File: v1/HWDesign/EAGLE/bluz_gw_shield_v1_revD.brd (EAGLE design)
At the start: 66 x 43.2 mm, 21 parts, among them J2 USB-MICROB, Q1 FC-12M, U2 MDBT40SMD, U3 SST25VF040B-S2, U4 SPARK_CORE

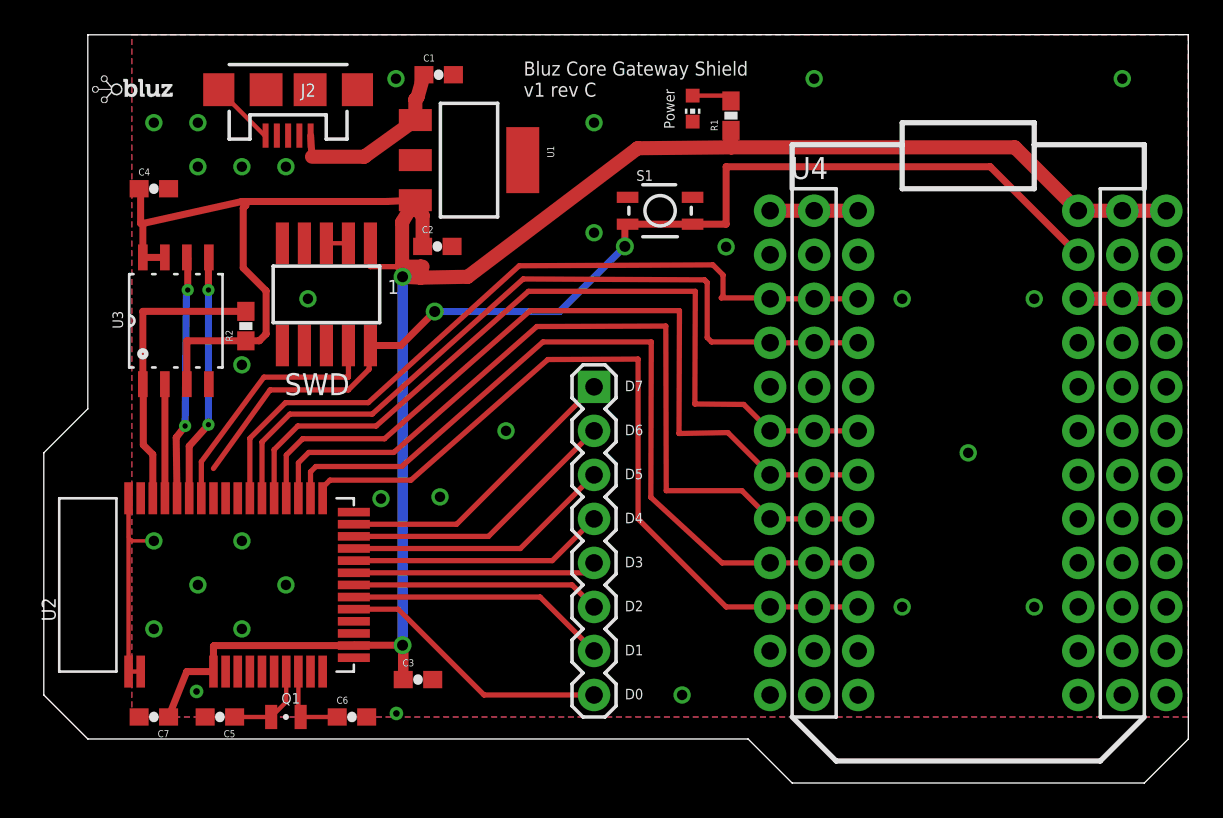
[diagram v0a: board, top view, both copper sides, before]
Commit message: newest files from adding the LED on D7 and TX/RX pins
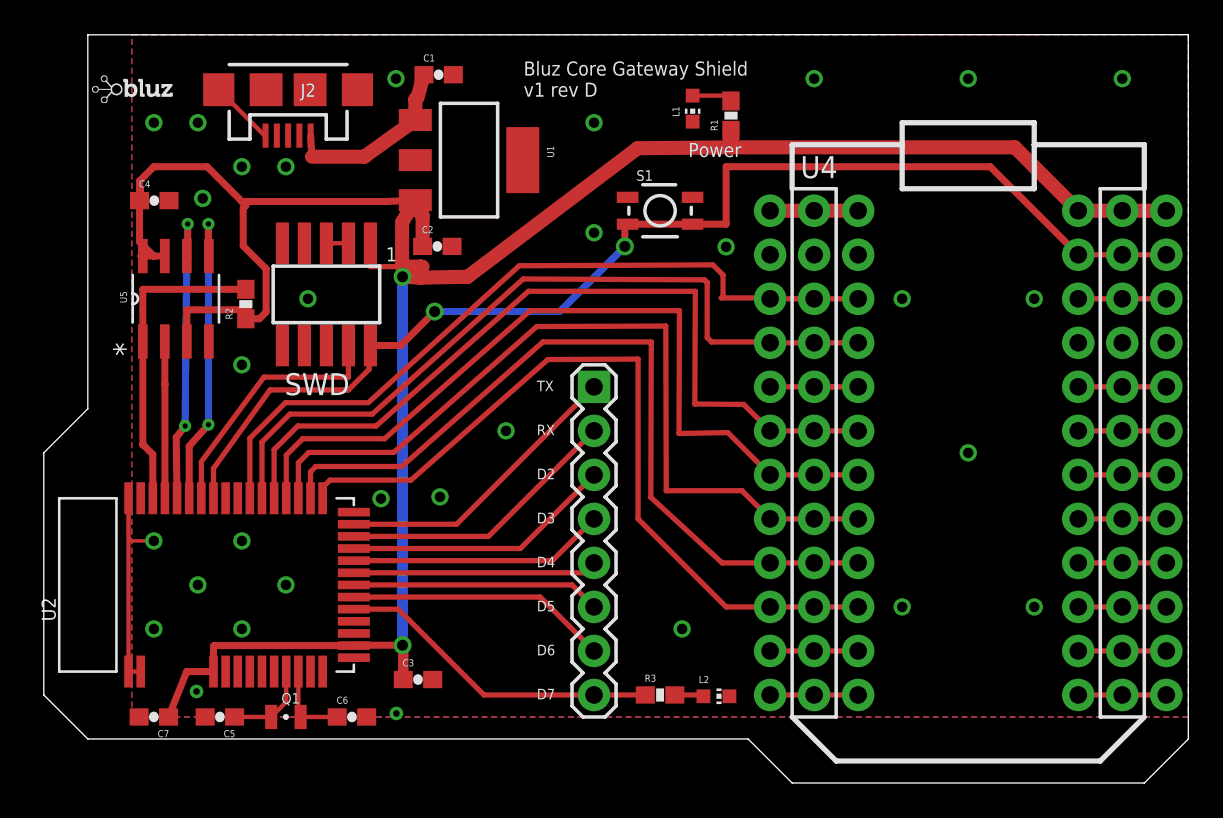
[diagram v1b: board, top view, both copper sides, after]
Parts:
- removed U3: SST25VF040B-S2, Spark:SOIC127P790X216-8N
- added L2: (no value), led:CHIP-LED0603
- added R3: 1k, SparkFun-Passives:0603-RES
- added U5: SST25VF010A-33-4I-SAE, Silicon_Storage_Tech_By_element14_Batch_1:SOIC127P600X175-8N
- moved R2 1.27 mm to (11.7, 27.6)
- moved C4 0.69 mm to (6.38, 33.6)
- renumbered LED1 to L1
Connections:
- net VDDA renamed N$17
- removed net D0: JP6.8, U2.17
- removed net D1: JP6.7, U2.18
- new net N$10: U4.#14, U4.14, U4.@14
- new net N$11: U4.#15, U4.15, U4.@15
- new net N$12: U4.#16, U4.16, U4.@16
- new net N$13: U4.#17, U4.17, U4.@17
- new net N$14: U4.#18, U4.18, U4.@18
- new net N$15: U4.#19, U4.19, U4.@19
- new net N$16: U4.#20, U4.20, U4.@20
- new net N$2: L2.A, R3.2
- new net N$3: U4.#5, U4.5, U4.@5
- new net N$4: U4.#11, U4.11, U4.@11
- new net N$6: U4.#12, U4.12, U4.@12
- new net N$9: U4.#13, U4.13, U4.@13
- new net NRF_RX: JP6.2, U2.23
- new net NRF_TX: JP6.1, U2.24
- net D2: now also JP6.3, U2.22; no longer JP6.6, U2.19
- net D3: now also JP6.4, U2.21; no longer JP6.5, U2.20
- net D4: now also JP6.5, U2.20; no longer JP6.4, U2.21
- net D5: now also JP6.6, U2.19; no longer JP6.3, U2.22
- net D6: now also JP6.7, U2.18; no longer JP6.2, U2.23
- net D7: now also JP6.8, R3.1, U2.17; no longer JP6.1, U2.24
- net GND: now also L2.C, U5.4; no longer U3.4
- net SPI_MISO: now also U5.2; no longer U3.2
- net SPI_MOSI: now also U5.5; no longer U3.5
- net SPI_SCK: now also U5.6; no longer U3.6
- net SPI_SS: now also U5.1; no longer U3.1
- net VCC: now also U5.3, U5.7, U5.8; no longer U3.3, U3.7, U3.8
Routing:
- net NRF_TX: track 0.00 -> 17.1 mm
- net NRF_RX: track 0.00 -> 16.4 mm
- net D0: track 15.9 -> 0.00 mm
- net D1: track 15.1 -> 0.00 mm
- net RST: track 63.0 -> 69.8 mm
- net N$3: track 0.00 -> 6.35 mm
- net N$6: track 0.00 -> 5.08 mm
- net N$4: track 0.00 -> 5.08 mm
- net N$9: track 0.00 -> 5.08 mm
- net N$16: track 0.00 -> 5.08 mm
- net N$15: track 0.00 -> 5.08 mm
- net N$14: track 0.00 -> 5.08 mm
- net N$13: track 0.00 -> 5.08 mm
- net N$12: track 0.00 -> 5.08 mm
- net N$11: track 0.00 -> 5.08 mm
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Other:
- board text added: "Bluz Core Gateway Shield v1 rev D"
- board text added: "RX"
- board text added: "TX"
- board text removed: "Bluz Core Gateway Shield v1 rev C"
- board text removed: "D0"
- board text removed: "D1"
